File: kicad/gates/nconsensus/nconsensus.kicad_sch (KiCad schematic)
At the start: 10 parts, among them J1 Conn_01x03, J2 Conn_01x03, Q1 BSS8402DW-7-F, Q2 BSS8402DW-7-F

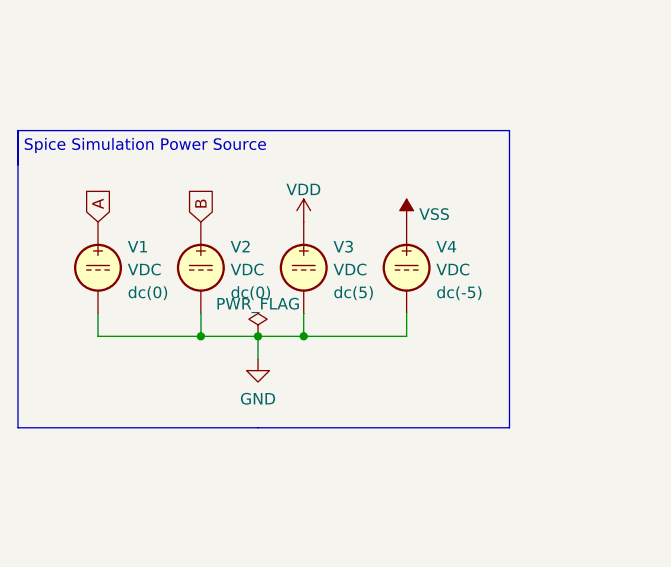
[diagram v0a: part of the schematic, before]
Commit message: update to kicad 9
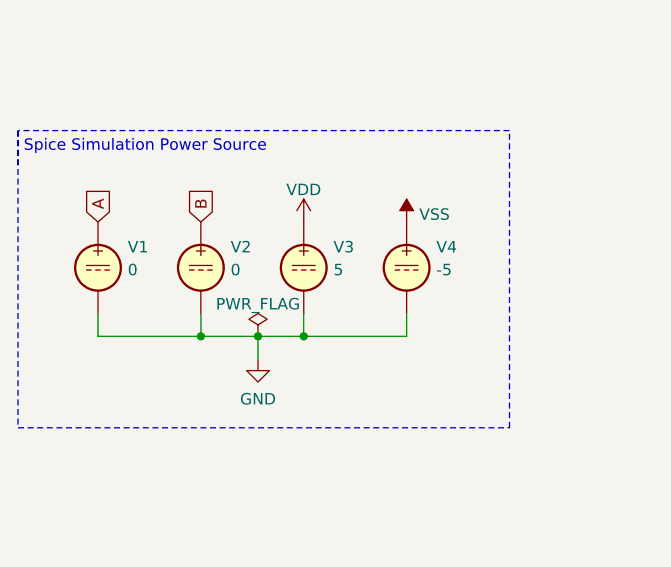
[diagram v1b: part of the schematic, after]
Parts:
- J1, J2: Spice_Model Conn_01x03 -> (none); Spice_Netlist_Enabled N -> (none); Spice_Primitive J -> (none)
- Q1, Q2: Spice_Lib_File /lab/dev/tritium/library/TritiumSpice.lib -> (none); Spice_Model BSS8402DW -> (none); Spice_Netlist_Enabled Y -> (none); Spice_Primitive X -> (none)
- V1, V2: value VDC -> 0; Spice_Model dc(0) -> (none); Spice_Netlist_Enabled Y -> (none); Spice_Primitive V -> (none)
- V3: value VDC -> 5; Spice_Model dc(5) -> (none); Spice_Netlist_Enabled Y -> (none); Spice_Primitive V -> (none)
- V4: value VDC -> -5; Spice_Model dc(-5) -> (none); Spice_Netlist_Enabled Y -> (none); Spice_Primitive V -> (none)
